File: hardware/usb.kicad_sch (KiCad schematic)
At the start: 11 parts, among them J8 USB-C, SW1 RESET, U3 USBLC6-2SC6, Y1 8MHz CL=20pF

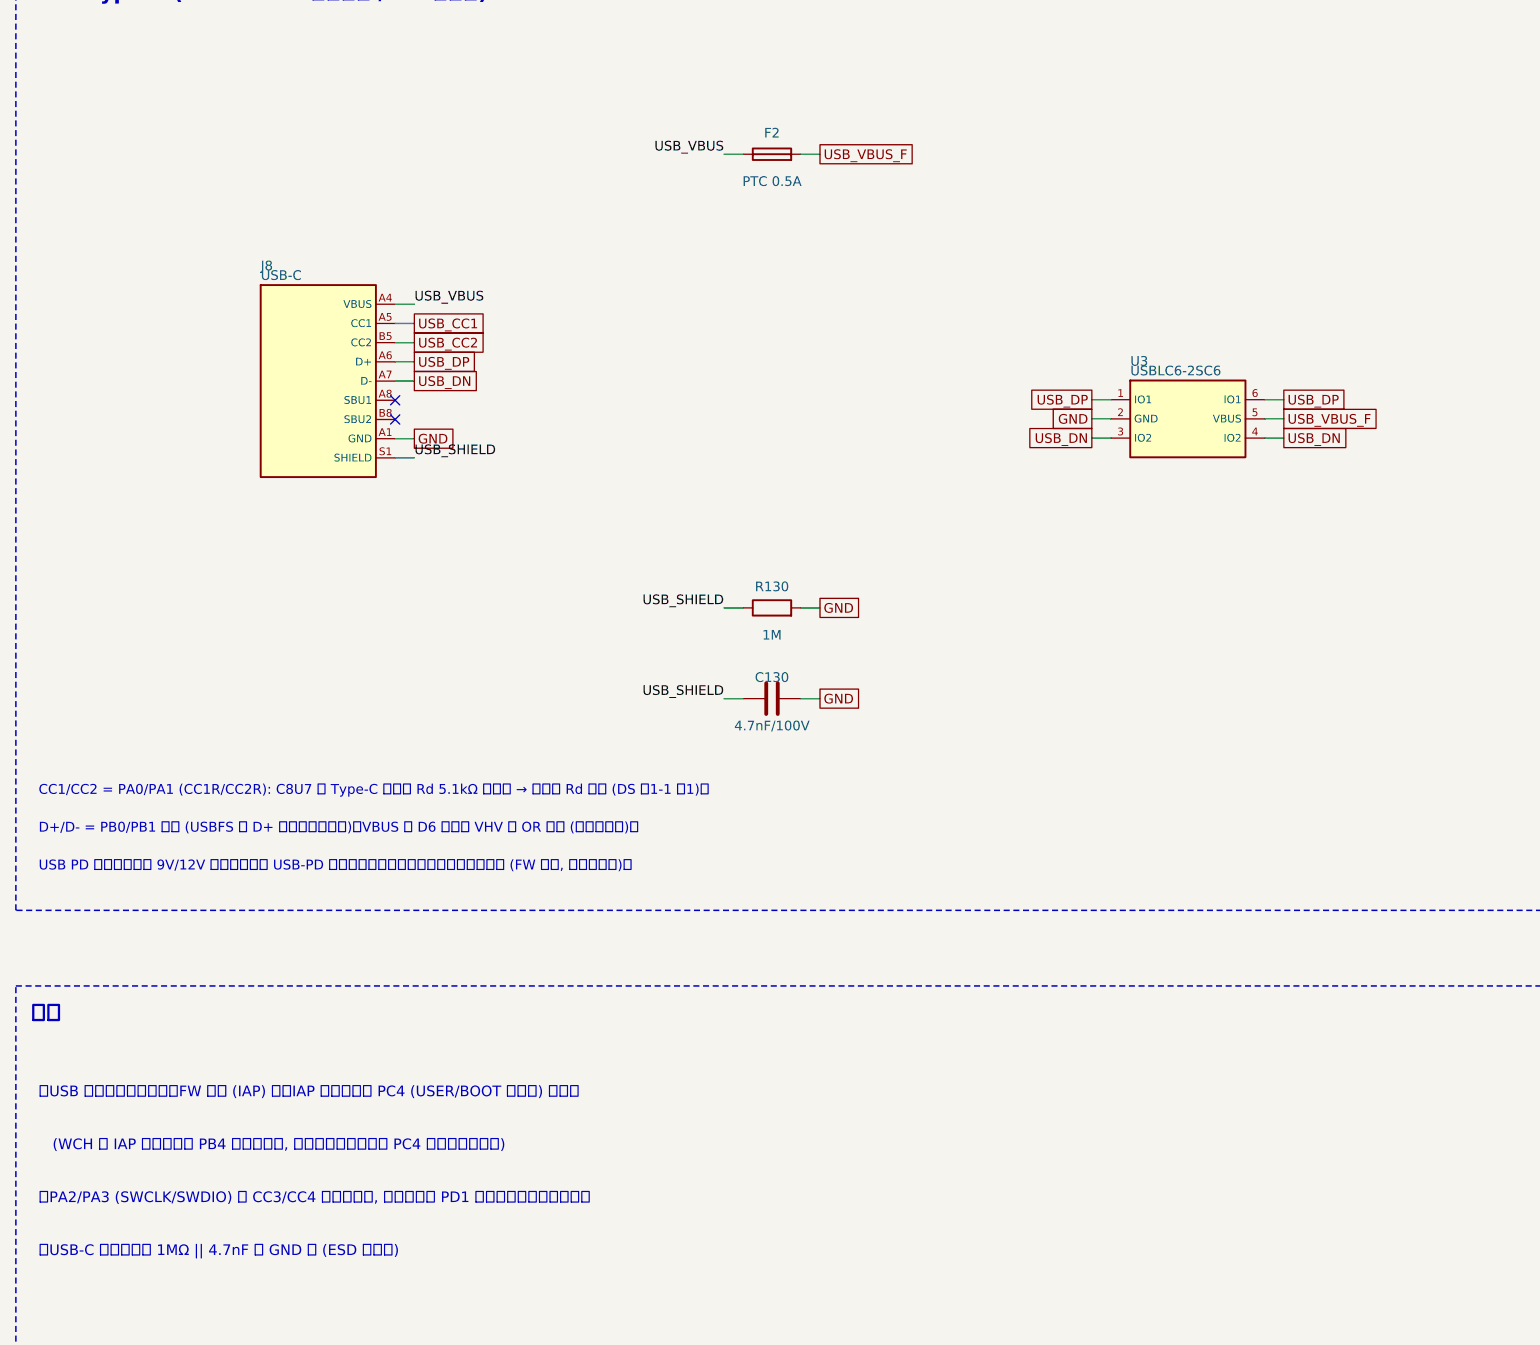
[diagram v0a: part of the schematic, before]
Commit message: Rev 0.2: 内蔵機能 (電流源/シンク・USB-PD・OPA/CMP 全モード) の活用
回路 (102/102 ネット一致):
- USB-PD シンクでモーター電源を供給: F3 → U5 LM74700 + Q10 → VBUS (PC3 で許可),
  USB VBUS 監視 (PA2), SMAJ20A。USBLC6 の基準を +3V3 に変更 (VBUS 20V 対策)
- J1 の逆接保護を U4 LM74700 + Q9 のハイサイド理想ダイオードに変更 (J1 / PD を安全に OR)
- 3 相センシングを PA5/PA6/PA7 に集約 (W 相 PA12 → PA6): CMP3 内部仮想中性点 + TIM2 捕捉
  によるセンサレス BEMF 検出, TIM2 ホール XOR, ISOURCE2 結線診断を同じピンで利用
- JP7: OPA3 入力を HB0 レッグ / バス電流で切替 (CMP2 + DAC でバス過電流・電流制限)
- JP8 + C105: QII1 (OPA1 → CMP1 → TIM3) でタコ / VR センサ / ブラシ DC 電流リップル計数
- 状態 LED を PC4 (USER/BOOT) と共用, J6/J7 を再割当 (1 線 SDI)

ファームウェア (警告 0):
- mpb.h ライブラリ: PD シンク (WCH USBPD_SNK 移植 + 8〜15V ポリシー + 給電パス制御),
  過電流保護 (CMP3/CMP2+DAC, TIM2 停止割込み), BEMF, ホール, タコ, NTC, 結線自己診断, TIM3 時間基準
- ブートローダ / テンプレートの状態 LED を PC4 (オープンドレイン) に変更

ドキュメント: docs/advanced_features.md (検討と判断, 要実機確認事項, Rev 0.3 候補)

Co-Authored-By: Claude Opus 5.5 <noreply@anthropic.com>
Claude-Session: https://claude.ai/code/session_01LENFjjhDfYjJZV1NWhB9uV
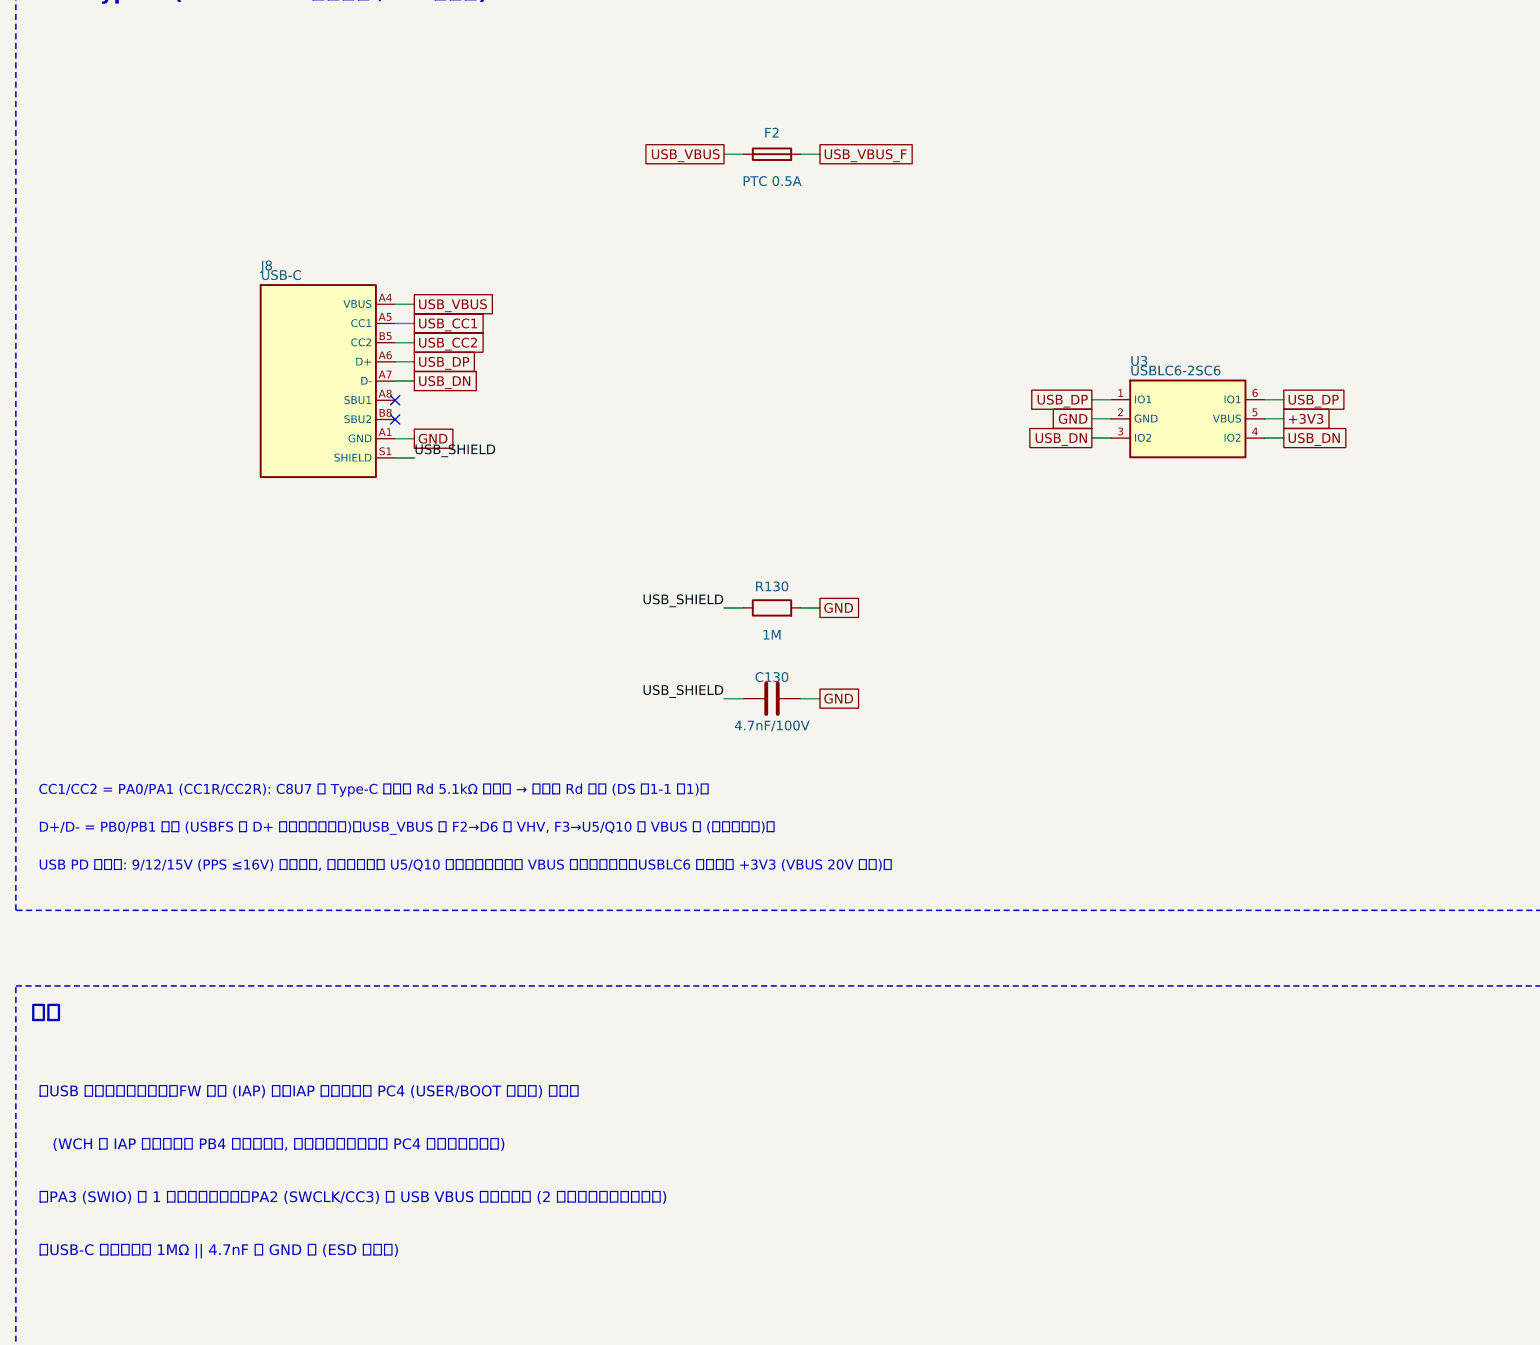
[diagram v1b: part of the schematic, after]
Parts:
- U3: MPN USBLC6-2SC6 (D+/D- ESD 保護) -> USBLC6-2SC6 (D+/D- ESD 保護, 基準は +3V3)
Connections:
- net +3V3: now also U3.5 (VBUS)
- net USB_VBUS_F: no longer U3.5 (VBUS)
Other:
- note added: "D+/D- = PB0/PB1 直結 (USBFS の D+ プルアップ内蔵)。USB_VBUS は F2→D6 で VHV, F3→U5/Q10 で VBUS へ (電源シート)。"
- note added: "USB PD シンク: 9/12/15V (PPS ≤16V) を要求し, 電源シートの U5/Q10 経由でモータ電源 VBUS に供給できる。USBLC6 の基準は +3V3 (VBUS 20V 対策)。"
- note added: "・PA3 (SWIO) は 1 線デバッグ専用。PA2 (SWCLK/CC3) は USB VBUS 監視に転用 (2 線デバッグは使わない)"
- note removed: "D+/D- = PB0/PB1 直結 (USBFS の D+ プルアップ内蔵)。VBUS は D6 経由で VHV に OR 接続 (電源シート)。"
- note removed: "USB PD シンクとして 9V/12V を要求すれば USB-PD 充電器からモータ電源を得る拡張も可能 (FW 次第, 要電流検討)。"
- note removed: "・PA2/PA3 (SWCLK/SWDIO) は CC3/CC4 と兼用だが, 本基板では PD1 側は使わずデバッグ専用"
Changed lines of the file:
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@@
 (kicad_sch (version 20230121) (generator eeschema)
 (paper "A3")
-(title_block (title "mPBCH32M030DS0  CH32M030 Universal Motor Driver") (date "2026-09-24") (rev "0.1") (company "ghostinkoma") (comment 1 "USB Type-C / 水晶発振子 / リセット") (comment 2 "個人利用可 (クレジット表示必須) / 商用利用は要連絡 / 無保証  -  LICENSE 参照"))
+(title_block (title "mPBCH32M030DS0  CH32M030 Universal Motor Driver") (date "2026-09-24") (rev "0.2") (company "ghostinkoma") (comment 1 "USB Type-C / 水晶発振子 / リセット") (comment 2 "個人利用可 (クレジット表示必須) / 商用利用は要連絡 / 無保証  -  LICENSE 参照"))
 (rectangle (start 20 25) (end 250 150) (stroke (width 0.2) (type dash)) (fill (type none)))
 (text "USB Type-C (USB2.0 FS デバイス / PD シンク)" (at 22 30 0) (effects (font (size 2 2) (thickness 0.3) bold) (justify left bottom)))
@@
 (text "メモ" (at 22 165 0) (effects (font (size 2 2) (thickness 0.3) bold) (justify left bottom)))
 (text "CC1/CC2 = PA0/PA1 (CC1R/CC2R): C8U7 は Type-C 規定の Rd 5.1kΩ を内蔵 → 外付け Rd 不要 (DS 表1-1 注1)。" (at 23 135 0) (effects (font (size 1.3 1.3)) (justify left bottom)))
-(text "D+/D- = PB0/PB1 直結 (USBFS の D+ プルアップ内蔵)。VBUS は D6 経由で VHV に OR 接続 (電源シート)。" (at 23 140 0) (effects (font (size 1.3 1.3)) (justify left bottom)))
-(text "USB PD シンクとして 9V/12V を要求すれば USB-PD 充電器からモータ電源を得る拡張も可能 (FW 次第, 要電流検討)。" (at 23 145 0) (effects (font (size 1.3 1.3)) (justify left bottom)))
+(text "D+/D- = PB0/PB1 直結 (USBFS の D+ プルアップ内蔵)。USB_VBUS は F2→D6 で VHV, F3→U5/Q10 で VBUS へ (電源シート)。" (at 23 140 0) (effects (font (size 1.3 1.3)) (justify left bottom)))
+(text "USB PD シンク: 9/12/15V (PPS ≤16V) を要求し, 電源シートの U5/Q10 経由でモータ電源 VBUS に供給できる。USBLC6 の基準は +3V3 (VBUS 20V 対策)。" (at 23 145 0) (effects (font (size 1.3 1.3)) (justify left bottom)))
 (text "XI=PB5 / XO=PB6。帰還抵抗は内蔵 (DS 表3-9)。C = 2 x (CL - 浮遊容量 約5pF) = 30pF。" (at 263 90 0) (effects (font (size 1.3 1.3)) (justify left bottom)))
 (text "HSE 8MHz x PLL18 = 144MHz → SYSCLK 72MHz / USB 48MHz。水晶の真下は GND ベタ, 配線は最短。" (at 263 95 0) (effects (font (size 1.3 1.3)) (justify left bottom)))
@@
 (text "・USB は設定変更・ログ・FW 更新 (IAP) 用。IAP 起動判定は PC4 (USER/BOOT ボタン) を使う" (at 23 175 0) (effects (font (size 1.4 1.4)) (justify left bottom)))
 (text "   (WCH の IAP サンプルは PB4 判定なので, 自作ブートローダで PC4 に変更すること)" (at 23 182 0) (effects (font (size 1.4 1.4)) (justify left bottom)))
-(text "・PA2/PA3 (SWCLK/SWDIO) は CC3/CC4 と兼用だが, 本基板では PD1 側は使わずデバッグ専用" (at 23 189 0) (effects (font (size 1.4 1.4)) (justify left bottom)))
+(text "・PA3 (SWIO) は 1 線デバッグ専用。PA2 (SWCLK/CC3) は USB VBUS 監視に転用 (2 線デバッグは使わない)" (at 23 189 0) (effects (font (size 1.4 1.4)) (justify left bottom)))
 (text "・USB-C シールドは 1MΩ || 4.7nF で GND へ (ESD 逃がし)" (at 23 196 0) (effects (font (size 1.4 1.4)) (justify left bottom)))
 (symbol (lib_id "mdrv:USBC16") (at 60 80 0) (unit 1) (in_bom yes) (on_board yes) (dnp no)
@@
 )
 (wire (pts (xy 70.16 69.84) (xy 72.7 69.84)) (stroke (width 0) (type default)))
-(label "USB_VBUS" (at 72.7 69.84 0) (fields_autoplaced) (effects (font (size 1.27 1.27)) (justify left bottom)))
+(global_label "USB_VBUS" (shape passive) (at 72.7 69.84 0) (fields_autoplaced) (effects (font (size 1.27 1.27)) (justify left)) (property "Intersheetrefs" "${INTERSHEET_REFS}" (at 72.7 69.84 0) (effects (font (size 1.27 1.27)) hide)))
 (wire (pts (xy 70.16 72.38) (xy 72.7 72.38)) (stroke (width 0) (type default)))
 (global_label "USB_CC1" (shape passive) (at 72.7 72.38 0) (fields_autoplaced) (effects (font (size 1.27 1.27)) (justify left)) (property "Intersheetrefs" "${INTERSHEET_REFS}" (at 72.7 72.38 0) (effects (font (size 1.27 1.27)) hide)))
@@
 )
 (wire (pts (xy 116.19 50) (xy 113.65 50)) (stroke (width 0) (type default)))
-(label "USB_VBUS" (at 113.65 50 180) (fields_autoplaced) (effects (font (size 1.27 1.27)) (justify right bottom)))
+(global_label "USB_VBUS" (shape passive) (at 113.65 50 180) (fields_autoplaced) (effects (font (size 1.27 1.27)) (justify right)) (property "Intersheetrefs" "${INTERSHEET_REFS}" (at 113.65 50 0) (effects (font (size 1.27 1.27)) hide)))
 (wire (pts (xy 123.81 50) (xy 126.35 50)) (stroke (width 0) (type default)))
 (global_label "USB_VBUS_F" (shape passive) (at 126.35 50 0) (fields_autoplaced) (effects (font (size 1.27 1.27)) (justify left)) (property "Intersheetrefs" "${INTERSHEET_REFS}" (at 126.35 50 0) (effects (font (size 1.27 1.27)) hide)))
@@
 (property "Footprint" "Package_TO_SOT_SMD:SOT-23-6" (at 175 85 0) (effects (font (size 1.27 1.27)) hide))
 (property "Datasheet" "~" (at 175 85 0) (effects (font (size 1.27 1.27)) hide))
-(property "MPN" "USBLC6-2SC6 (D+/D- ESD 保護)" (at 175 85 0) (effects (font (size 1.27 1.27)) hide))
+(property "MPN" "USBLC6-2SC6 (D+/D- ESD 保護, 基準は +3V3)" (at 175 85 0) (effects (font (size 1.27 1.27)) hide))
 (pin "1")
 (pin "2")
@@
 (global_label "USB_DP" (shape passive) (at 187.7 82.46 0) (fields_autoplaced) (effects (font (size 1.27 1.27)) (justify left)) (property "Intersheetrefs" "${INTERSHEET_REFS}" (at 187.7 82.46 0) (effects (font (size 1.27 1.27)) hide)))
 (wire (pts (xy 185.16 85) (xy 187.7 85)) (stroke (width 0) (type default)))
-(global_label "USB_VBUS_F" (shape passive) (at 187.7 85 0) (fields_autoplaced) (effects (font (size 1.27 1.27)) (justify left)) (property "Intersheetrefs" "${INTERSHEET_REFS}" (at 187.7 85 0) (effects (font (size 1.27 1.27)) hide)))
+(global_label "+3V3" (shape passive) (at 187.7 85 0) (fields_autoplaced) (effects (font (size 1.27 1.27)) (justify left)) (property "Intersheetrefs" "${INTERSHEET_REFS}" (at 187.7 85 0) (effects (font (size 1.27 1.27)) hide)))
 (wire (pts (xy 185.16 87.54) (xy 187.7 87.54)) (stroke (width 0) (type default)))
 (global_label "USB_DN" (shape passive) (at 187.7 87.54 0) (fields_autoplaced) (effects (font (size 1.27 1.27)) (justify left)) (property "Intersheetrefs" "${INTERSHEET_REFS}" (at 187.7 87.54 0) (effects (font (size 1.27 1.27)) hide)))

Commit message: Rev 0.3: パワー段を子基板化 (A/B/C/D) し 2 層基板レイアウトを作成
構成:
- 主基板 (60x42mm, 2 層): 右 = CH32M030 / USB-C / GPIO・I2C・UART・SDI・HALL,
  左上 = 電源 (J1 → F1 → 理想ダイオード, USB-PD 経路), 左下 = 基板間コネクタ J9/J10 (裏面)
- 子基板と裏面同士を背中合わせに重ねる (基板間 約5mm, 裏面部品は高さ 2mm 以下)。
  RESET / USER・BOOT / センシング選択は主基板 TOP、電流チャネル選択 JP5/JP7 は子基板 TOP
- 子基板 A: TPN1R603PL (既存回路) / B: TKR74F04PB (24V 系, 66x66mm) /
  C: MTN2306AN3 (廉価版) / D: MOSFET なし (全信号をピンヘッダへ引き出し)
- 基板間ピンは同じ番号同士が嵌合 (ソケットを 270° 回転して裏面実装, 座標で全 32 ピンを検証)
- コネクタは USB-C 以外すべて 2.54mm ピンヘッダ。コンデンサは 1005/1608 基本
  (入手性を確認した量産品番。50V/10uF のみ 2012)
- 24V 対応: Q9 を 40V 品 (TPN2R304PL), VHV に 47Ω + 27V ツェナー, D1/R11 の 24V 用定数を注記,
  FW は make POWER_STAGE=B で VBUS 分圧比を切替
- F1 を NANO2 10A (SMD), スイッチを B3U-1000P に小型化

基板生成 (hardware/gen_pcb.py + pcblib.py):
- 配置 → Freerouting 1.9 自動配線 → 大電流ネットのベタ化 → GND ベタ・スティッチング
  → 残り接続の補修 (格子 A*, DRC が増えない経路のみ採用) → DRC
- 5 基板とも未接続 0・電気的 DRC エラー 0 (警告はシルクの重なりのみ)
- 製造データ hardware/fab/*.zip (ガーバー, ドリル, 両面の部品座標)

回路図: 主基板 82/82, 子基板 A/B/C 41/41, D 21/21 ネット一致。FW は A/B とも警告 0 でビルド。

Co-Authored-By: Claude Opus 5.5 <noreply@anthropic.com>
Claude-Session: https://claude.ai/code/session_01LENFjjhDfYjJZV1NWhB9uV
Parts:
- C130: footprint Capacitor_SMD:C_0603_1608Metric -> Capacitor_SMD:C_0402_1005Metric; MPN (none) -> Murata GRM155R72A472KA01D (X7R 1005)
- C131, C132: MPN (none) -> Murata GRM1555C1H300JA01D (C0G 1005)
- C133: value 0.1uF -> 0.1uF/50V; MPN (none) -> Murata GRM155R71H104KE14D (X7R 1005)
- F2: MPN ポリスイッチ 0.5A 1206 -> ポリスイッチ 0.5A 1206 (例: Bourns MF-NSMF050)
- SW1: footprint Button_Switch_SMD:SW_SPST_TL3342 -> Button_Switch_SMD:SW_SPST_B3U-1000P; MPN タクトスイッチ -> Omron B3U-1000P (3x2.5mm SMD タクト, 上押し)
- U3: MPN USBLC6-2SC6 (D+/D- ESD 保護, 基準は +3V3) -> ST USBLC6-2SC6 (D+/D- ESD 保護, 基準は +3V3)
- Y1: MPN 8MHz 3225 4pad, CL=20pF, ESR≤60Ω -> 8MHz 3225 4pad, CL=20pF, ESR≤60Ω (例: Abracon ABM8-8.000MHZ-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
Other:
- note added: "CC1/CC2 = PA0/PA1 (CC1R/CC2R): C8U7 は Type-C 規定の Rd 5.1kΩ を内蔵 → 外付け Rd 不要。"
- note added: "D+/D- = PB0/PB1 直結 (USBFS の D+ プルアップ内蔵)。USB_VBUS は F2→D6 で VHV, F3→U5/Q10 で VBUS へ。"
- note added: "USB PD シンク: 9/12/15V を要求し U5/Q10 経由でモータ電源 VBUS に供給できる。"
- note added: "XI=PB5 / XO=PB6。帰還抵抗は内蔵。C = 2 x (CL - 浮遊容量 約5pF) = 30pF。"
- note added: "リセット (RST = PC0) ※ TOP 面"
- note added: "・PA3 (SWIO) は 1 線デバッグ専用。PA2 (SWCLK/CC3) は USB VBUS 監視に転用"
- note added: "・USB は設定変更・ログ・FW 更新 (IAP) 用。IAP 起動判定は PC4 (USER/BOOT ボタン)"
- note added: "・USB-C は主基板の右辺 (MCU 近傍)。PD 給電パス F3/U5/Q10 は左上の電源エリアへ太パターンで接続"
- note removed: "(WCH の IAP サンプルは PB4 判定なので, 自作ブートローダで PC4 に変更すること)"
- note removed: "CC1/CC2 = PA0/PA1 (CC1R/CC2R): C8U7 は Type-C 規定の Rd 5.1kΩ を内蔵 → 外付け Rd 不要 (DS 表1-1 注1)。"
- note removed: "D+/D- = PB0/PB1 直結 (USBFS の D+ プルアップ内蔵)。USB_VBUS は F2→D6 で VHV, F3→U5/Q10 で VBUS へ (電源シート)。"
- note removed: "USB PD シンク: 9/12/15V (PPS ≤16V) を要求し, 電源シートの U5/Q10 経由でモータ電源 VBUS に供給できる。USBLC6 の基準は +3V3 (VBUS 20V 対策)。"
- note removed: "XI=PB5 / XO=PB6。帰還抵抗は内蔵 (DS 表3-9)。C = 2 x (CL - 浮遊容量 約5pF) = 30pF。"
- note removed: "リセット (RST = PC0)"
- note removed: "・PA3 (SWIO) は 1 線デバッグ専用。PA2 (SWCLK/CC3) は USB VBUS 監視に転用 (2 線デバッグは使わない)"
- note removed: "・USB は設定変更・ログ・FW 更新 (IAP) 用。IAP 起動判定は PC4 (USER/BOOT ボタン) を使う"
- title: mPBCH32M030DS0  CH32M030 Universal Motor Driver -> mPBCH32M030DS0  CH32M030 Universal Motor Driver - Main board

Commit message: Rev 0.4: DIP-42 MCU module + power boards A/B/C (KiCad 8)
- MCU module: 20.32 x 53.34mm (8 x 21 grid), DIP-42 (0.6in rows), fits
  an 82 x 52mm breadboard. Headers can be fitted from either side;
  signal names on bottom silk. All LEDs (power, status, 8 gate LEDs) on
  the module top.
- Power boards take the module in two 1x21 sockets (left/right
  symmetric mating). FETs/shunts on the heatsink side, no LEDs.
  Voltage-dependent parts (TVS, OVP divider, bulk caps, BEMF divider)
  moved to the power boards. Breakout board D removed.
  A/C: 20.32 x 71.94mm, B (TO-263 x8): 40.64 x 66.94mm.
- Capacitors re-selected for realistic size vs voltage/capacitance
  (4.7uF 1608, 10uF/25V 2012, 10uF/50V 1206, 4.7nF/100V 1608, low
  profile electrolytics).
- Schematics and boards generated in KiCad 8 format; netlists verified
  with KiCad 8.0.9.
- Layout pipeline: Freerouting bridge (parallel), second pass, early
  repair before pours, island-aware maze repair, DRC via kicad-cli.
- DRC: power boards A/B/C have 0 unconnected / 0 electrical errors.
  The MCU module still has unrouted connections (work in progress).

Co-Authored-By: Claude Opus 5.5 <noreply@anthropic.com>
Claude-Session: https://claude.ai/code/session_01LENFjjhDfYjJZV1NWhB9uV
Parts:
- C130: footprint Capacitor_SMD:C_0402_1005Metric -> Capacitor_SMD:C_0603_1608Metric; MPN Murata GRM155R72A472KA01D (X7R 1005) -> Samsung CL10B472KC8NNNC (X7R 100V 1608)
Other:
- note added: "CC1/CC2 = PA0/PA1 (Rd 5.1kΩ 内蔵)。D+/D- = PB0/PB1。USB_VBUS は J1-1/2 (子基板の PD 給電経路) へ。"
- note added: "RST ピンはユーザオプションバイトで有効化 (RST_PIN_SEL=0 → PC0)。"
- note added: "XI=PB5 / XO=PB6。C = 2 x (CL - 浮遊容量 約5pF) = 30pF。"
- note added: "リセット (RST = PC0) ※ 上面"
- note added: "注意: PD 契約後は USB_VBUS が 9〜15V になる。ブレッドボードでは USB_VBUS ピンに 5V 部品を直結しないこと。"
- note removed: "(WCH-LinkUtility で設定, 出荷時は無効の可能性)。無効時は PC0 は通常 GPIO。"
- note removed: "CC1/CC2 = PA0/PA1 (CC1R/CC2R): C8U7 は Type-C 規定の Rd 5.1kΩ を内蔵 → 外付け Rd 不要。"
- note removed: "D+/D- = PB0/PB1 直結 (USBFS の D+ プルアップ内蔵)。USB_VBUS は F2→D6 で VHV, F3→U5/Q10 で VBUS へ。"
- note removed: "HSE 8MHz x PLL18 = 144MHz → SYSCLK 72MHz / USB 48MHz。水晶の真下は GND ベタ, 配線は最短。"
- note removed: "RST ピンはユーザオプションバイトで選択: RST_PIN_SEL=0 → PC0, RST_MODE で有効化"
- note removed: "USB PD シンク: 9/12/15V を要求し U5/Q10 経由でモータ電源 VBUS に供給できる。"
- note removed: "XI=PB5 / XO=PB6。帰還抵抗は内蔵。C = 2 x (CL - 浮遊容量 約5pF) = 30pF。"
- note removed: "メモ"
- note removed: "リセット (RST = PC0) ※ TOP 面"
- note removed: "・PA3 (SWIO) は 1 線デバッグ専用。PA2 (SWCLK/CC3) は USB VBUS 監視に転用"
- note removed: "・USB は設定変更・ログ・FW 更新 (IAP) 用。IAP 起動判定は PC4 (USER/BOOT ボタン)"
- note removed: "・USB-C は主基板の右辺 (MCU 近傍)。PD 給電パス F3/U5/Q10 は左上の電源エリアへ太パターンで接続"
- note removed: "・USB-C シールドは 1MΩ || 4.7nF で GND へ (ESD 逃がし)"
- title: mPBCH32M030DS0  CH32M030 Universal Motor Driver - Main board -> mPBCH32M030DS0  CH32M030 motor-driver MCU module (DIP-42)
